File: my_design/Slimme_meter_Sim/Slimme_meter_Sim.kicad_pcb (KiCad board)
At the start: 2 copper layers, 117.3 x 143.1 mm, 99 parts, among them CN1 S2B-PH-SM4-TB, SW1 MSK12C02, SW2 KMR231GLFS, U1 USBLC6-2SC6-ES, U2 BQ25185DLHR, U3 TPS61023DRLR, U4 TPS26625DRCR, U5 C1206C105K3RACAUTO, U6 SY8088AAC, U7 ESP32-C3-MINI-1-H4X, U8 6N137S_C20612601, U9 6N137S_C20612601

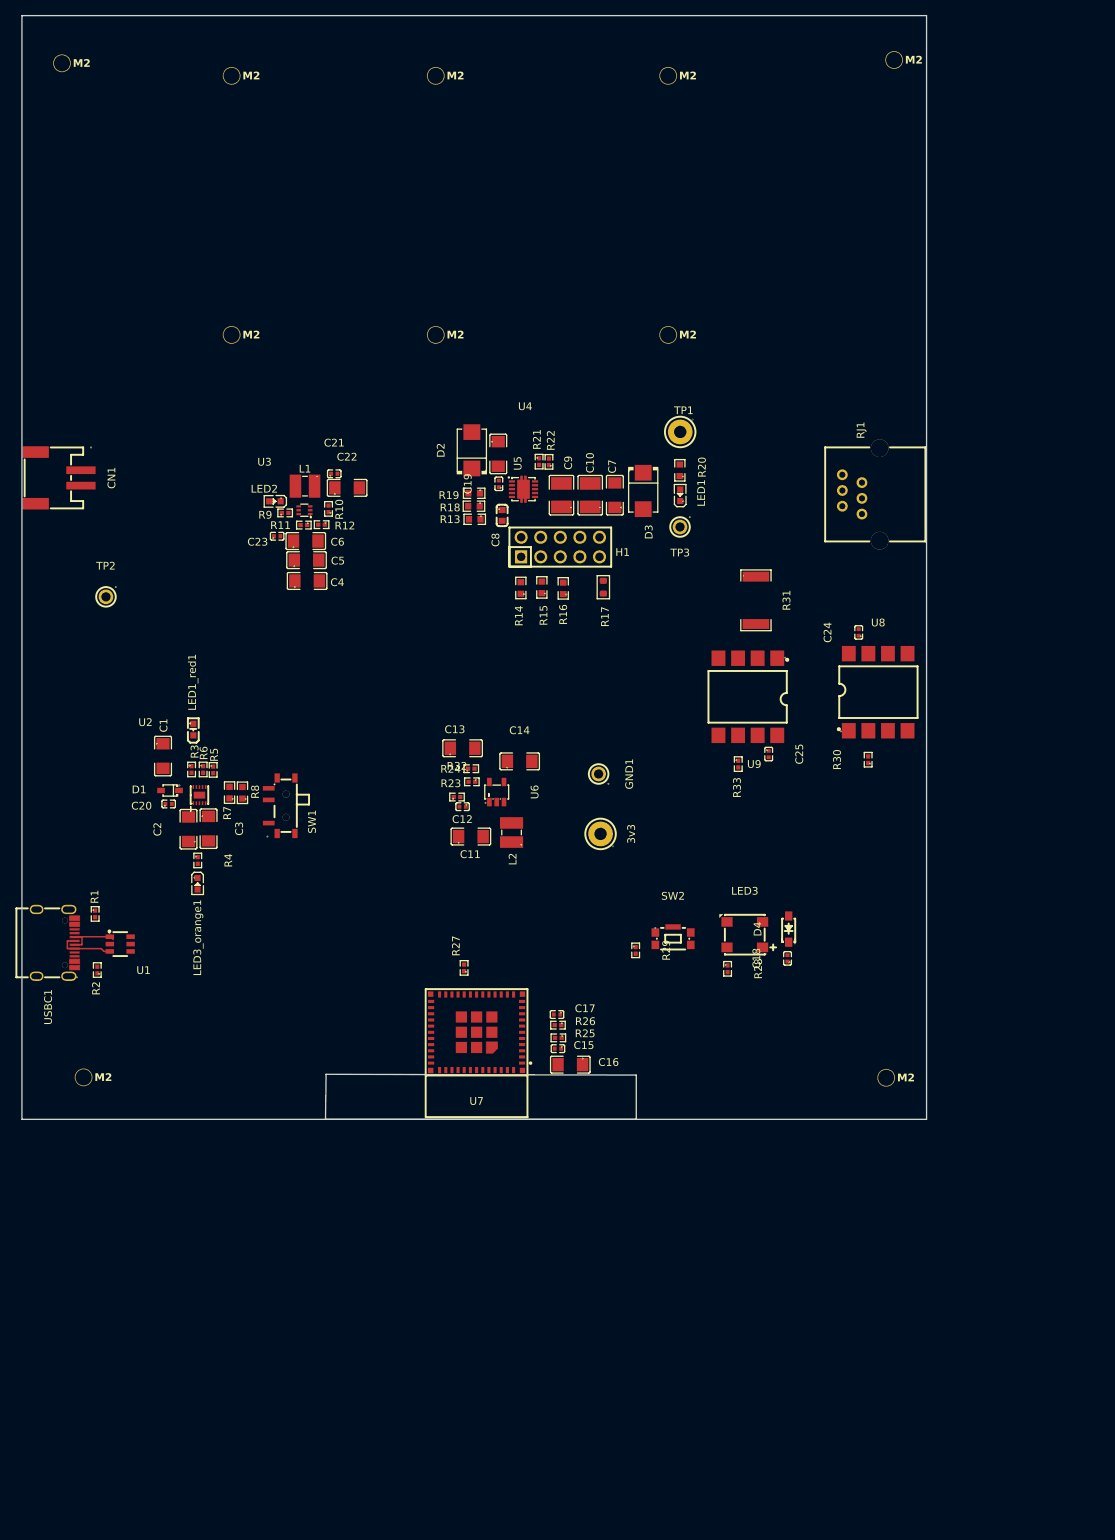
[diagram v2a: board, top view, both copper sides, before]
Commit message: Save Slimme_meter_Sim KiCad progress: PCB/schematic, footprints, and firmware pin map.
Co-authored-by: Cursor <cursoragent@cursor.com>
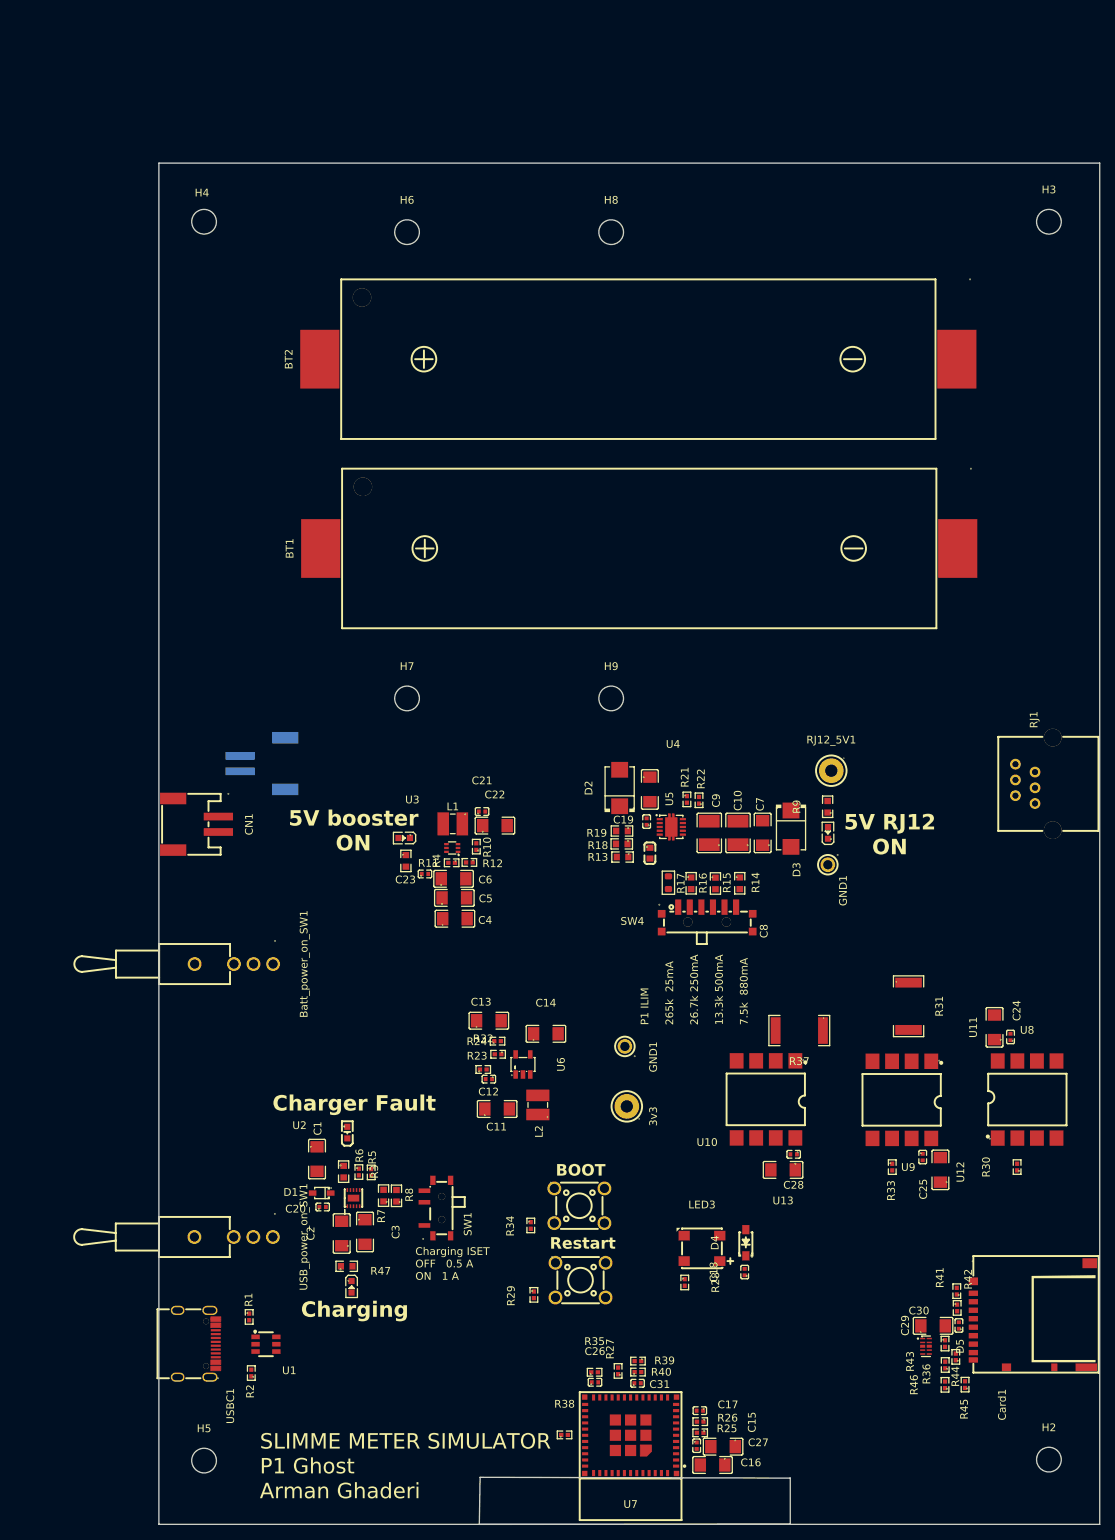
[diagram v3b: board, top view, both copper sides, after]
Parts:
- removed H1: DS1023-2*5SF11, EasyEDA:HDR-TH_10P-P2.54-V-F-R2-C5-S2.54
- removed H10, H11: ~, PCM_fab:MountingHole_M2
- removed R20: AR03FTC2672, EasyEDA:R0603
- removed TP1: RH-5117, EasyEDA:TESTPOINT-TH_BD3.2-D1.6
- removed TP2: RH-5002, EasyEDA:TESTPOINT-TH_BD2.5-D1.2_RH-5002
- added BT1: BH-18650-B1BA002, EasyEDA:BATTERY-SMD_18650-1S-L77.1-W20.7-1, F.Cu at (132.4, 87.7)
- added BT2: BH-18650-B1BA002, EasyEDA:BATTERY-SMD_18650-1S-L77.1-W20.7-1, F.Cu at (132.3, 63.2)
- added Batt_power_on_SW1: ST-0-102-C04-N008-RS, EasyEDA:SW-TH_ST-0-102-C04-N008-RS, F.Cu at (79.8, 141.6)
- added C26: CL05A105KA5NQNC, EasyEDA:C0402, F.Cu at (126.7, 195.9)
- added C27: FS31X226M160EPG, EasyEDA:C1206, F.Cu at (143.3, 204.2)
- added C28: CL05B104KO5NNNC, EasyEDA:C0402, F.Cu at (152.4, 166.3)
- added C29: CL05B104KO5NNNC, EasyEDA:C0402, F.Cu at (173.9, 188.5)
- added C30: FS31X226M160EPG, EasyEDA:C1206, F.Cu at (170.5, 188.6)
- added C31: CL05B104KO5NNNC, EasyEDA:C0402, F.Cu at (132.2, 196.0)
- added CN2: S2B-PH-SM4-TB, EasyEDA:CONN-SMD_P2.00_S2B-PH-SM4-TB-LF-SN, B.Cu at (83.6, 115.6)
- added Card1: DM3AT-SF-PEJM5, EasyEDA:SD-SMD_DM3AT-SF-PEJM5, F.Cu at (183.3, 187.2)
- added D5: RCLAMP0524P_C907837, EasyEDA:DFN2510-10_L2.5-W1.0-P0.50-BL, F.Cu at (169.6, 191.2)
- added R34: AR02BTC1002, EasyEDA:R0402, F.Cu at (118.3, 175.5)
- added R35: AR02BTC1002, EasyEDA:R0402, F.Cu at (126.6, 194.6)
- added R36: AR02BTC1002, EasyEDA:R0402, F.Cu at (172.1, 193.6)
- added R37: 25121WJ0331T4E, EasyEDA:R2512, F.Cu at (153.2, 150.2)
- added R38: AR02BTC1002, EasyEDA:R0402, F.Cu at (122.7, 202.7)
- added R39: 0402WGF1003TCE, EasyEDA:R0402, F.Cu at (132.2, 193.1)
- added R40: 0402WGF1003TCE, EasyEDA:R0402, F.Cu at (132.2, 194.5)
- added R41: AR02BTC1002, EasyEDA:R0402, F.Cu at (173.6, 184.1)
- added R42: AR02BTC1002, EasyEDA:R0402, F.Cu at (173.7, 186.2)
- added R43: AR02BTC1002, EasyEDA:R0402, F.Cu at (172.1, 190.8)
- added R44: AR02BTC1002, EasyEDA:R0402, F.Cu at (173.5, 192.6)
- added R45: AR02BTC1002, EasyEDA:R0402, F.Cu at (174.7, 196.2)
- added R46: AR02BTC1002, EasyEDA:R0402, F.Cu at (172.1, 196.2)
- added R47: RC0603JR-071KL, EasyEDA:R0603, F.Cu at (94.5, 180.8)
- added RJ12_5V1: RH-5117, EasyEDA:TESTPOINT-TH_BD3.2-D1.6, F.Cu at (157.3, 116.5)
- added SW3: TS665CJ, EasyEDA:SW-TH_4P-L6.0-W6.0-P4.50-LS6.5, F.Cu at (124.7, 173.0)
- added SW4: SK-1500-L1?, EasyEDA:SW-SMD_6P-P1.50_L2.7-W11.2, F.Cu at (141.2, 135.8)
- added U10: 6N137S_C20612601, EasyEDA:SOP-8_L9.7-W6.5-P2.54-LS10.3-BL, F.Cu at (148.9, 159.2)
- added U11: C1206C105K3RACAUTO, EasyEDA:C1206, F.Cu at (178.5, 149.8)
- added U12: C1206C105K3RACAUTO, EasyEDA:C1206, F.Cu at (171.5, 168.3)
- added U13: C1206C105K3RACAUTO, EasyEDA:C1206, F.Cu at (151.1, 168.3)
- added USB_power_on_SW1: ST-0-102-C04-N008-RS, EasyEDA:SW-TH_ST-0-102-C04-N008-RS, F.Cu at (79.8, 177.0)
- H2, H3, H4, H5, H6, H7, H8, H9: footprint PCM_fab:MountingHole_M2 -> MountingHole:MountingHole_3.2mm_M3
- R3, R4: value AR02BTC5101 -> RC0603JR-071KL; footprint EasyEDA:R0402 -> EasyEDA:R0603
- R9: value AR02BTC1002 -> RC0603JR-071KL; footprint EasyEDA:R0402 -> EasyEDA:R0603
- SW2: value KMR231GLFS -> TS665CJ; footprint EasyEDA:KEY-SMD_KMR2XXGXXX -> EasyEDA:SW-TH_4P-L6.0-W6.0-P4.50-LS6.5
- moved R9 80.0 mm to (156.8, 121.2), turned to 90 degrees
- moved R30 56.3 mm to (181.4, 168.0)
- moved U8 56.3 mm to (182.7, 159.2)
- moved R31 56.2 mm to (167.3, 147.1)
- moved C3 56.1 mm to (96.8, 176.4)
- moved R5 56.1 mm to (97.7, 168.7)
- moved C2 56.1 mm to (93.8, 176.6)
- moved C24 56.0 mm to (180.6, 151.1)
- moved R6 56.0 mm to (96.0, 168.6)
- moved LED1_red1 56.0 mm to (94.6, 163.5)
- moved LED3_orange1 56.0 mm to (95.1, 183.5)
- moved R1 56.0 mm to (81.8, 187.4)
- moved R27 56.0 mm to (129.7, 194.4)
- moved R33 56.0 mm to (165.2, 168.0)
- moved U2 56.0 mm to (95.4, 172.0)
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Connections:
- C17 pad 2: Net-(U7-EN) -> /SCH_2_power_supplies/ESP32_Sw
- CN1 pad 1: VBATT -> /SCH_1_USB_5volt/V_batt_port
- D1 pad 2: 5V_usb -> 5V_usb_1
- R26 pad 2: Net-(U7-EN) -> /SCH_2_power_supplies/ESP32_Sw
- R3 pad 1: Net-(LED1_red1-K) -> /SCH_1_USB_5volt/stat1
- R3 pad 2: /SCH_1_USB_5volt/stat1 -> Net-(LED1_red1-K)
- R4 pad 1: /SCH_1_USB_5volt/stat2 -> Net-(LED2-A)
- R4 pad 2: Net-(LED3_orange1-K) -> +5V
- R9 pad 1: Net-(LED2-A) -> Net-(LED1-A)
- R9 pad 2: +5V -> RJ12_5V
- U7 pad 12: unconnected-(U7-IO0-Pad12) -> /SCH_2_power_supplies/GPIO0_SCK
- U7 pad 13: unconnected-(U7-IO1-Pad13) -> /SCH_2_power_supplies/GPIO1_MOSI_CMD
- U7 pad 18: /SCH_2_power_supplies/ESP32_Sw -> /SCH_1_USB_5volt/GPIO4_Battery
- U7 pad 20: unconnected-(U7-IO6-Pad20) -> /SCH_2_power_supplies/GPIO6_CS
- U7 pad 21: unconnected-(U7-IO7-Pad21) -> /SCH_2_power_supplies/SD_CD_SW_A
- U7 pad 23: unconnected-(U7-IO9-Pad23) -> /SCH_2_power_supplies/ESP32_Sw_GPIO9
- U7 pad 30: unconnected-(U7-RXD0-Pad30) -> /SCH_2_power_supplies/ESP32_FLT_Efuse
- U7 pad 6: unconnected-(U7-IO3-Pad6) -> /SCH_2_power_supplies/GPIO3_MISO
- U7 pad 8: Net-(U7-EN) -> /SCH_2_power_supplies/ESP32_Sw
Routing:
- net /SCH_1_USB_5volt/usb_d-: track 7.85 -> 0.00 mm
- net /SCH_1_USB_5volt/usb_d+: track 7.55 -> 0.00 mm
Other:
- board size 117.3 x 143.1 mm -> 122 x 176.6 mm
- board text added: "5V RJ12 ON"
- board text added: "5V booster ON"
- board text added: "BOOT"
- board text added: "Charger Fault"
- board text added: "Charging"
- board text added: "Charging ISET OFF 0.5 A ON 1 A"
- board text added: "GND1"
- board text added: "P1 ILIM 265k 25mA 26.7k 250mA 13.3k 500mA 7.5k 880mA"
- board text added: "Restart"
- board text added: "SLIMME METER SIMULATOR P1 Ghost Arman Ghaderi"

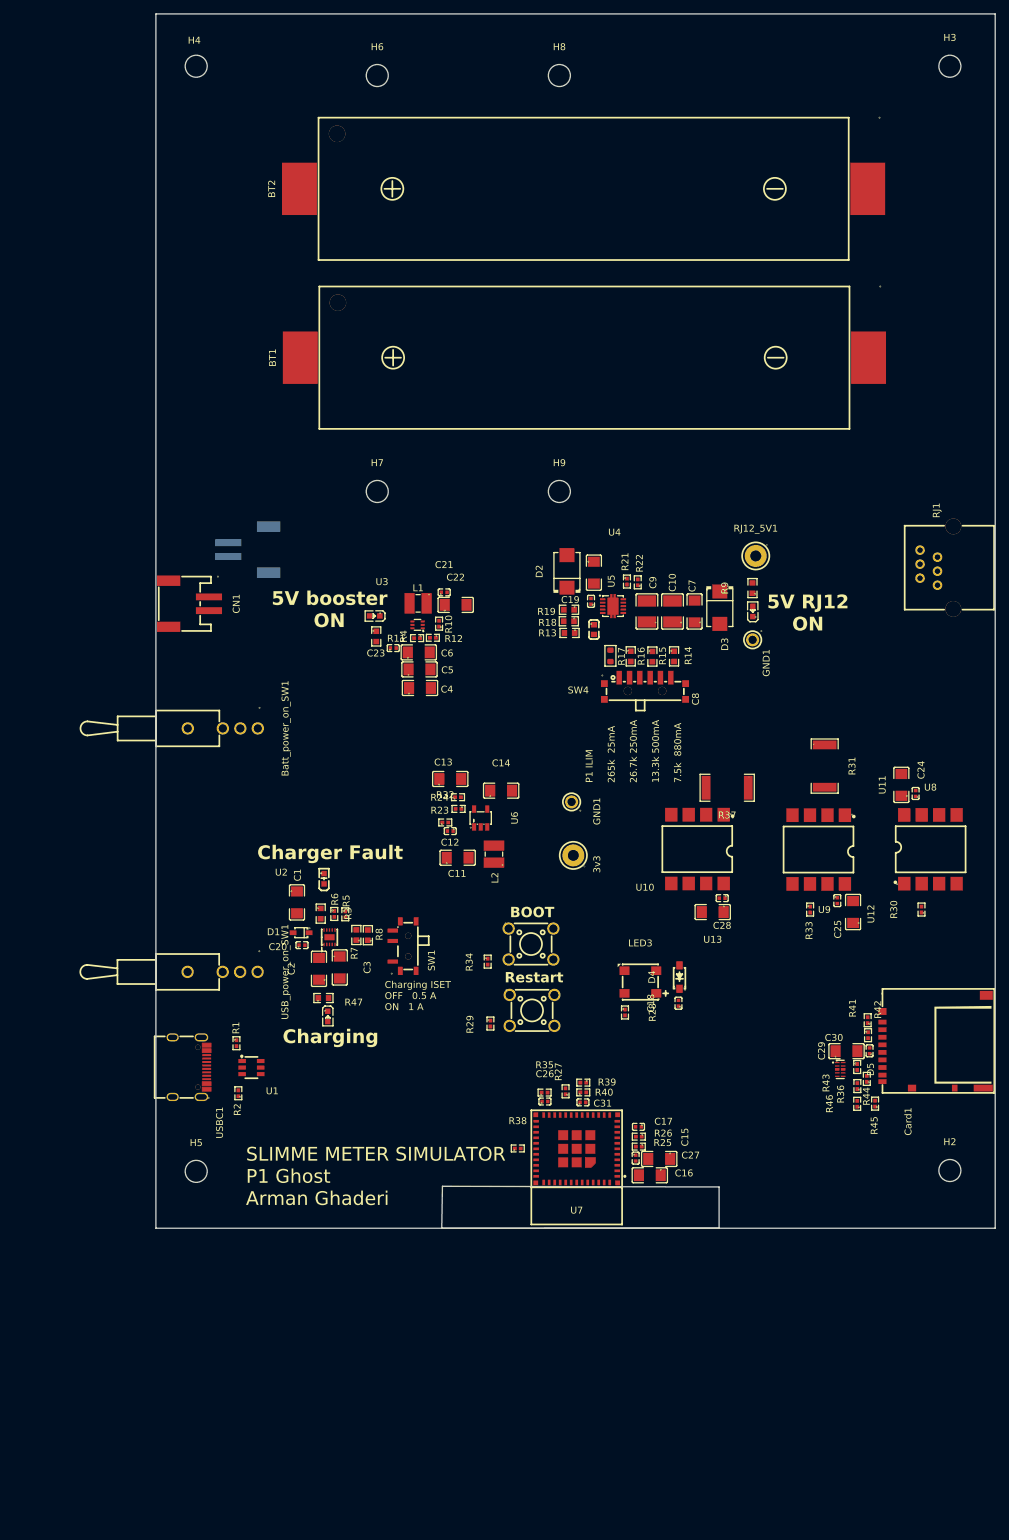
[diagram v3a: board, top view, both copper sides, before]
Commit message: Save production-ready Slimme_meter_Sim Gerbers, JLCPCB BOM/CPL, and finished PCB.
Co-authored-by: Cursor <cursoragent@cursor.com>
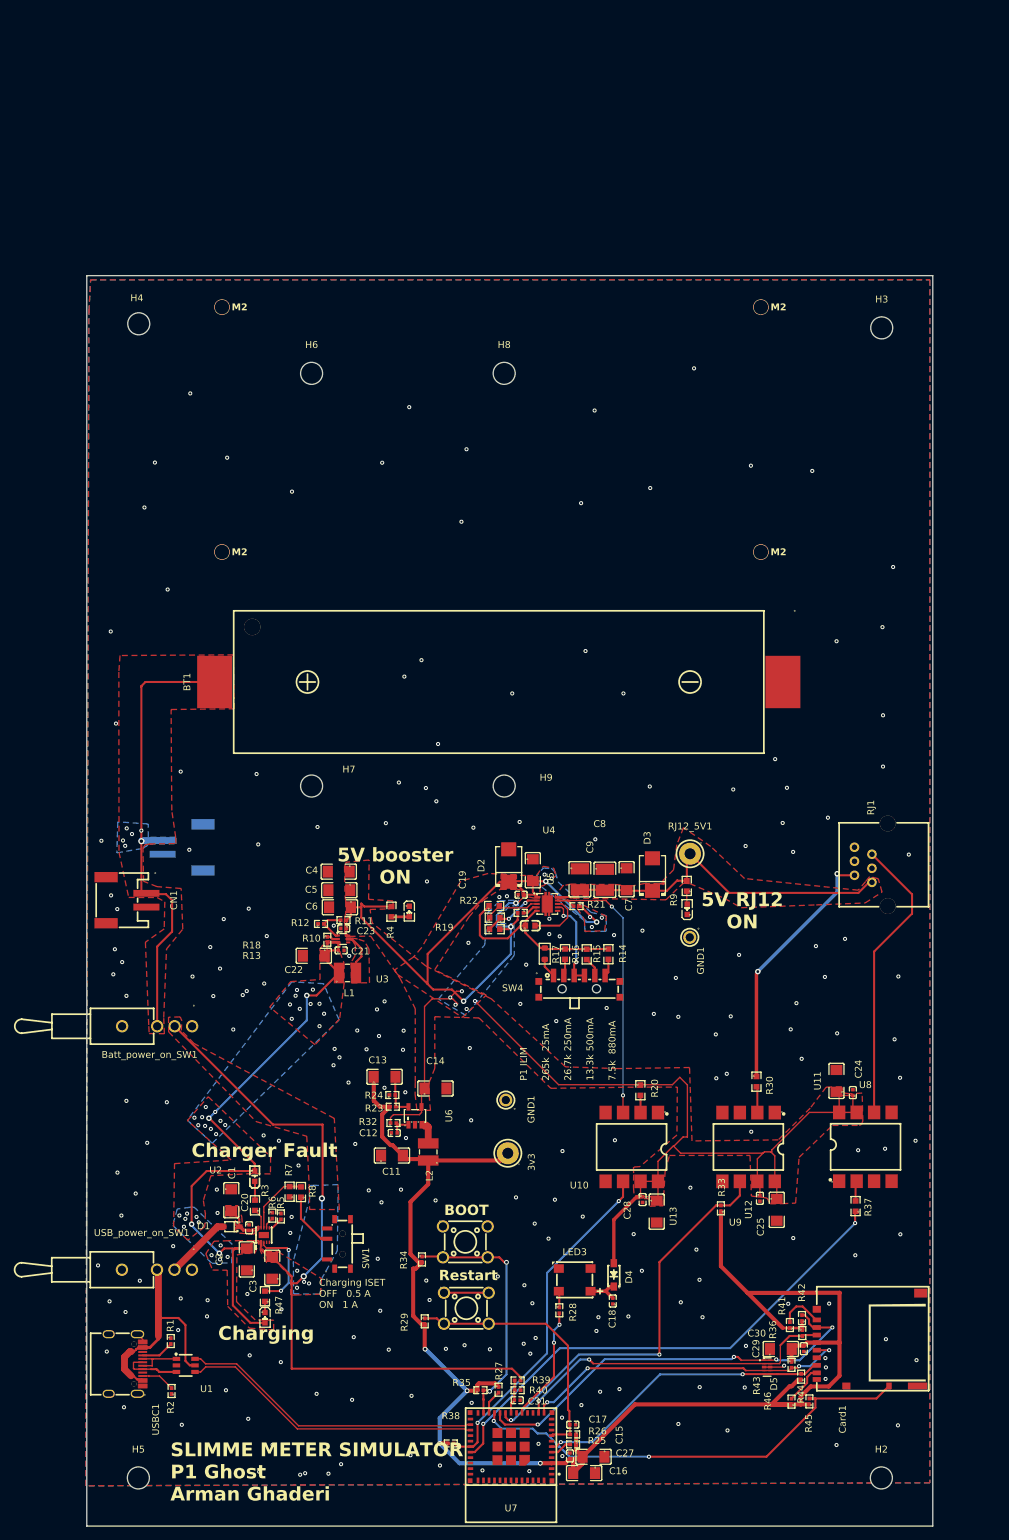
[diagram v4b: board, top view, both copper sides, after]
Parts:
- removed BT2: BH-18650-B1BA002, EasyEDA:BATTERY-SMD_18650-1S-L77.1-W20.7-1
- removed C26: CL05A105KA5NQNC, EasyEDA:C0402
- removed R31: 25121WJ0331T4E, EasyEDA:R2512
- added H1: ~, PCM_fab:MountingHole_M2, F.Cu at (79.7, 80.4)
- added H10: ~, PCM_fab:MountingHole_M2, F.Cu at (79.7, 116.0)
- added H11: ~, PCM_fab:MountingHole_M2, F.Cu at (158.1, 80.4)
- added H12: ~, PCM_fab:MountingHole_M2, F.Cu at (158.1, 116.0)
- added R20: ERJP03F3300V, EasyEDA:R0603, F.Cu at (140.6, 194.2)
- R30: value MCS04020C2200FE000 -> ERJP03F3300V; footprint EasyEDA:R0402 -> EasyEDA:R0603
- R37: value 25121WJ0331T4E -> 0603WAF2200T5E; footprint EasyEDA:R2512 -> EasyEDA:R0603
- moved R37 63.6 mm to (171.8, 211.1), turned to 90 degrees
- moved C22 55.0 mm to (93.1, 174.7), turned to 180 degrees
- moved L1 54.7 mm to (98.0, 177.2), turned to 0 degrees
- moved C21 54.2 mm to (97.0, 173.9)
- moved R22 51.0 mm to (123.1, 168.4), turned to 180 degrees
- moved BT1 48.8 mm to (120.0, 134.9)
- moved R10 48.7 mm to (95.0, 172.3), turned to -90 degrees
- moved R21 47.8 mm to (131.3, 167.5), turned to 180 degrees
- moved R19 47.7 mm to (119.4, 170.8), turned to 0 degrees
- moved U3 46.9 mm to (97.3, 172.2), turned to 180 degrees
- moved H2 45.8 mm to (175.6, 250.6)
- moved H5 45.4 mm to (67.6, 250.6)
- moved R33 45.3 mm to (152.3, 211.4), turned to 90 degrees
- moved C28 45.3 mm to (140.9, 210.1), turned to -90 degrees
- moved R5 44.9 mm to (88.3, 212.6)
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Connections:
- R21 pad 2: Net-(U4-~{FLT}) -> /SCH_2_power_supplies/Efuse_FLT
- R30 pad 1: /SCH_2_power_supplies/ESP32_TX -> /SCH_2_power_supplies/RJ12_pin2
- R30 pad 2: Net-(U8-AN) -> Net-(U9-AN)
- R37 pad 1: +5V -> /SCH_2_power_supplies/ESP32_TX
- R37 pad 2: Net-(U10-AN) -> Net-(U8-AN)
- U4 pad 9: Net-(U4-~{FLT}) -> /SCH_2_power_supplies/Efuse_FLT
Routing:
- net +5V: track 0.00 -> 262.7 mm, vias 0 -> 15
- net +3V3: track 0.00 -> 231.0 mm, vias 0 -> 4
- net VBATT: track 0.00 -> 107.6 mm, vias 0 -> 6
- net VCC: track 0.00 -> 94.4 mm, vias 0 -> 34
- net /SCH_2_power_supplies/ESP32_TX: track 0.00 -> 73.2 mm, vias 0 -> 2
- net /SCH_1_USB_5volt/V_batt_port: track 0.00 -> 68.4 mm, vias 0 -> 6
- net /SCH_2_power_supplies/SD_CD_SW_A: track 0.00 -> 67.7 mm, vias 0 -> 2
- net /SCH_2_power_supplies/GPIO6_CS: track 0.00 -> 61.5 mm, vias 0 -> 4
- net /SCH_2_power_supplies/ESP32_enable: track 0.00 -> 58.3 mm, vias 0 -> 2
- net RJ12_5V: track 0.00 -> 53.5 mm
- net /SCH_2_power_supplies/ESP32_FLT_Efuse: track 0.00 -> 50.6 mm, vias 0 -> 2
- net /SCH_2_power_supplies/GPIO1_MOSI_CMD: track 0.00 -> 48.1 mm, vias 0 -> 2
- net /SCH_2_power_supplies/GPIO0_SCK: track 0.00 -> 47.9 mm, vias 0 -> 4
- net USB_D-: track 0.00 -> 44.1 mm
- net USB_D+: track 0.00 -> 44.1 mm
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- added copper zone on B.Cu, net +5V
- added copper zone on F.Cu, net +5V
- added copper zone on B.Cu, net /SCH_1_USB_5volt/V_batt_port
- added copper zone on F.Cu, net /SCH_1_USB_5volt/V_batt_port
- added copper zone on B.Cu, net GND1
- added copper zone on F.Cu, net GND1
- added copper zone on F.Cu, net Net-(D1-C)
- added copper zone on F.Cu, net Net-(U3-SW)
- added copper zone on F.Cu, net RJ12_5V
- added copper zone on B.Cu, net VBATT
- added copper zone on F.Cu, net VBATT
- added copper zone on B.Cu, net VCC
- added copper zone on F.Cu, net VCC
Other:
- board size 122 x 176.6 mm -> 123 x 181.8 mm
